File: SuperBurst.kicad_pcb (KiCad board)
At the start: 2 copper layers, 40 x 20 mm, 8 parts, among them P1 CONN_01X03, P2 CONN_01X03, Q1 Si2301, Q2 Si2301

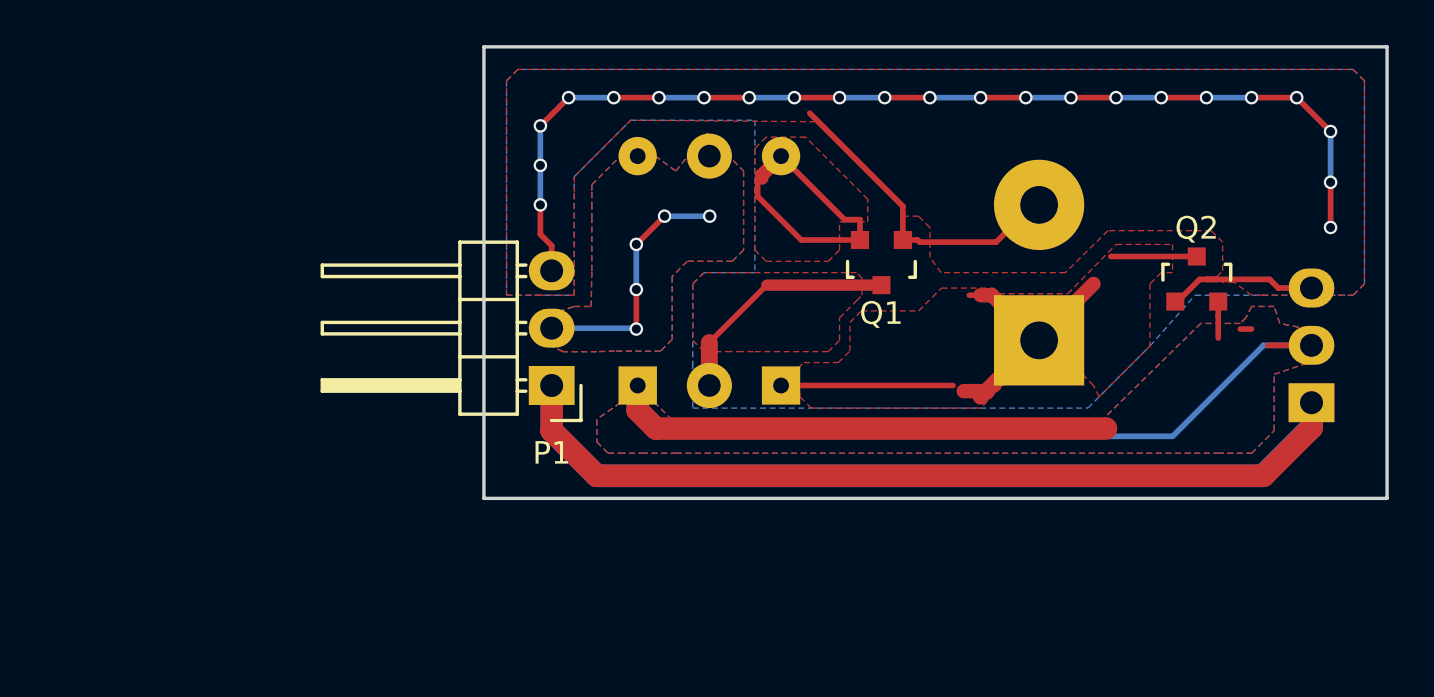
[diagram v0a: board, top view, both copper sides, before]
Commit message: Low ESR supercap with voltage detector
Advanced discrete component circuit that charges the supercap, then via
mosfets as switches, exposes the charged supercap to downstream loads.
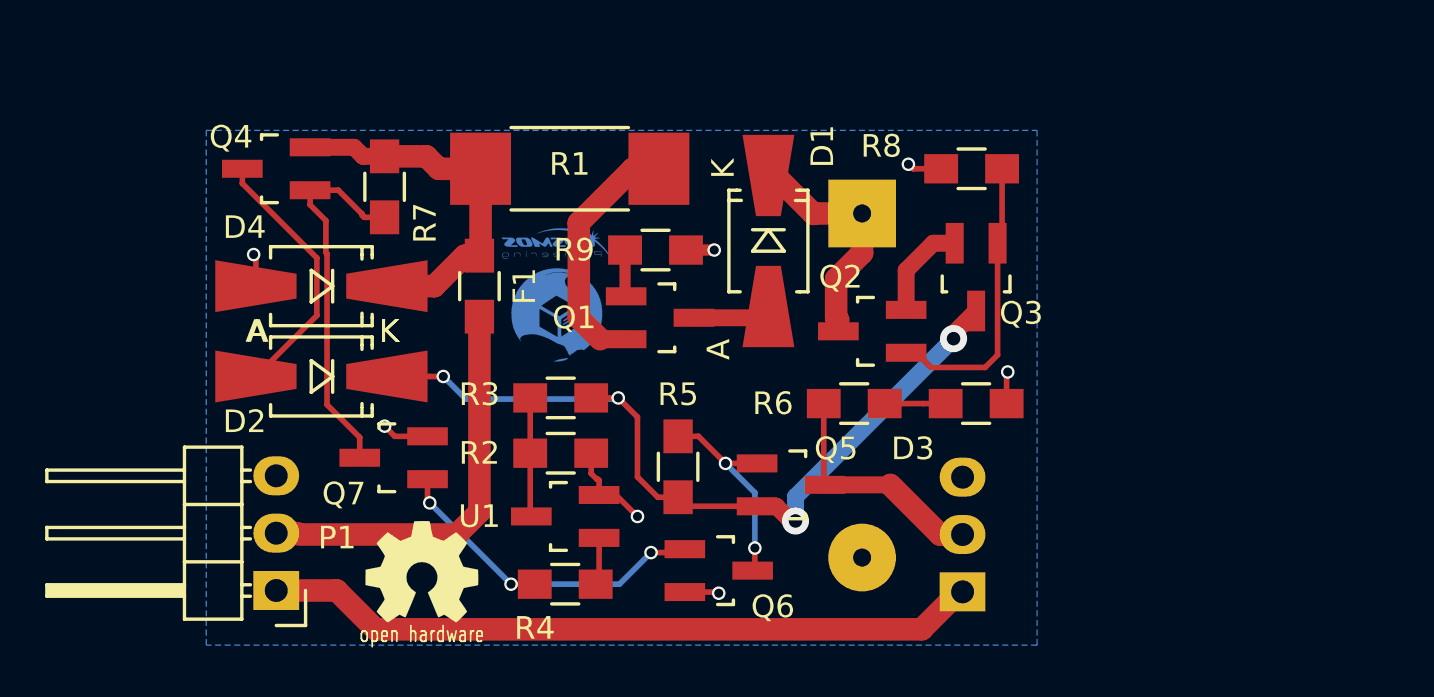
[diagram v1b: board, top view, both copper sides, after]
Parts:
- added ?: REF, CosmosLogo1:LOGO, B.Cu at (127.2, 106.0)
- added ?: LOGO, w_logo:Logo_silk_OSHW_6x6mm, F.Cu at (121.2, 117.5)
- added D3: LED, Resistors_SMD:R_0805_HandSoldering, F.Cu at (145.8, 110.0)
- added D4: ZENER, Diodes_SMD:SMA-SMB_Universal_Handsoldering, F.Cu at (116.8, 104.8)
- added F1: FUSE, Resistors_SMD:R_0805_HandSoldering, F.Cu at (123.8, 104.8)
- added Q3: Si2301, TO_SOT_Packages_SMD:SOT-23_Handsoldering, F.Cu at (145.8, 104.4)
- added Q4: Si2301, TO_SOT_Packages_SMD:SOT-23_Handsoldering, F.Cu at (114.8, 99.6)
- added Q5: Si2301, TO_SOT_Packages_SMD:SOT-23_Handsoldering, F.Cu at (137.6, 113.6)
- added Q6: PZT2222A, TO_SOT_Packages_SMD:SOT-23_Handsoldering, F.Cu at (134.4, 117.4)
- added Q7: PZT2222A, TO_SOT_Packages_SMD:SOT-23_Handsoldering, F.Cu at (120.0, 112.4)
- added R2: OPEN, Resistors_SMD:R_0805_HandSoldering, F.Cu at (127.4, 112.2)
- added R3: 0 Ohm, Resistors_SMD:R_0805_HandSoldering, F.Cu at (127.4, 109.8)
- added R4: 1K Ohm, Resistors_SMD:R_0805_HandSoldering, F.Cu at (127.6, 118.0)
- added R5: 10K Ohm, Resistors_SMD:R_0805_HandSoldering, F.Cu at (132.6, 112.8)
- added R6: 330 Ohm, Resistors_SMD:R_0805_HandSoldering, F.Cu at (140.4, 110.0)
- added R7: 10K Ohm, Resistors_SMD:R_0805_HandSoldering, F.Cu at (119.6, 100.4)
- added R8: 0 Ohm, Resistors_SMD:R_0805_HandSoldering, F.Cu at (145.6, 99.6)
- added R9: 0 Ohm, Resistors_SMD:R_0805_HandSoldering, F.Cu at (131.6, 103.2)
- added U1: TC54, TO_SOT_Packages_SMD:SOT-23_Handsoldering, F.Cu at (127.6, 115.0)
- C1: value 1.5F -> 0.47F (Low ESR)
- D1: value 1N4148 -> 1N5817; footprint Diodes_ThroughHole:Diode_DO-35_SOD27_Horizontal_RM10 -> Diodes_SMD:SMA-SMB_Universal_Handsoldering; moved to F.Cu
- D2: value 1N4001 -> 1N5817; footprint Diodes_ThroughHole:Diode_DO-35_SOD27_Horizontal_RM10 -> Diodes_SMD:SMA-SMB_Universal_Handsoldering; moved to F.Cu
- Q1, Q2: footprint TO_SOT_Packages_SMD:SOT-23 -> TO_SOT_Packages_SMD:SOT-23_Handsoldering
- R1: footprint Resistors_ThroughHole:Resistor_Horizontal_RM10mm -> Resistors_SMD:R_2512_HandSoldering; moved to F.Cu
- moved D2 20.4 mm to (116.8, 108.8), turned to 180 degrees
- moved P2 17.6 mm to (145.2, 118.4)
- moved P1 15.2 mm to (114.8, 118.3)
- moved Q2 14.6 mm to (141.2, 106.8), turned to 90 degrees
- moved R1 11.4 mm to (127.8, 99.6), turned to 0 degrees
- moved Q1 10.1 mm to (131.8, 106.2), turned to 270 degrees
- moved C1 9.30 mm to (140.8, 109.2), turned to 270 degrees
- moved D1 8.63 mm to (136.6, 102.8), turned to 270 degrees
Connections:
- net Net-(P1-Pad1) renamed PWMin
- D1 pad 1: +4V3 -> Net-(C1-Pad1)
- D1 pad 2: +5V -> Net-(D1-Pad2)
- D2 pad 1: Net-(C1-Pad1) -> Net-(D2-Pad1)
- P1 pad 2: +5V -> Net-(F1-Pad2)
- Q1 pad 1: GND -> Net-(Q1-Pad1)
- Q1 pad 2: Net-(D2-Pad2) -> Net-(Q1-Pad2)
- Q1 pad 3: Net-(Q1-Pad3) -> Net-(D1-Pad2)
- Q2 pad 1: GND -> Net-(Q2-Pad1)
- Q2 pad 2: +4V3 -> Net-(Q2-Pad2)
- R1 pad 1: Net-(Q1-Pad3) -> +5V
- R1 pad 2: +5V -> Net-(Q1-Pad2)
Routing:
- net GND: track 68.4 -> 13.4 mm, vias 23 -> 7
- net +4V3: track 59.6 -> 10.6 mm
- net PWMin: track 77.0 -> 31.8 mm
- net Net-(D2-Pad1): track 0.00 -> 36.2 mm, vias 0 -> 4
- net (no net): track 0.00 -> 27.6 mm
- net Net-(F1-Pad2): track 0.00 -> 18.1 mm
- net Net-(Q4-Pad1): track 0.00 -> 16.6 mm
- net Net-(Q6-Pad1): track 0.00 -> 15.6 mm, vias 0 -> 3
- net Net-(Q2-Pad1): track 0.00 -> 12.9 mm
- net Net-(C1-Pad1): track 23.0 -> 10.6 mm
- net Net-(Q1-Pad2): track 0.00 -> 11.2 mm
- net Net-(Q1-Pad3): track 10.6 -> 0.00 mm
- net Net-(Q5-Pad1): track 0.00 -> 9.33 mm, vias 0 -> 2
- net Net-(R2-Pad1): track 0.00 -> 5.27 mm
- net +5V: track 11.3 -> 16.5 mm, vias 5 -> 0
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- removed copper zone on B.Cu, net +4V3
- removed copper zone on F.Cu, net +4V3
- removed copper zone on B.Cu, net +5V
- removed copper zone on F.Cu, net +5V
- removed copper zone on F.Cu, net GND
- removed copper zone on F.Cu, net Net-(C1-Pad1)
- removed copper zone on F.Cu, net Net-(D2-Pad2)
- removed copper zone on F.Cu, net Net-(Q1-Pad3)
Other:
- board outline removed

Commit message: First Load
Initial load of the board
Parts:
- P2: footprint Pin_Headers:Pin_Header_Angled_1x03 -> SuperCap:Pin_Header_Angled_1x03B
